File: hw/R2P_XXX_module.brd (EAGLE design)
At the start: 40 x 40 mm, 32 parts, among them U1 STM32F103CX, U5 LD3985XX, X1 MICROMATCH-4

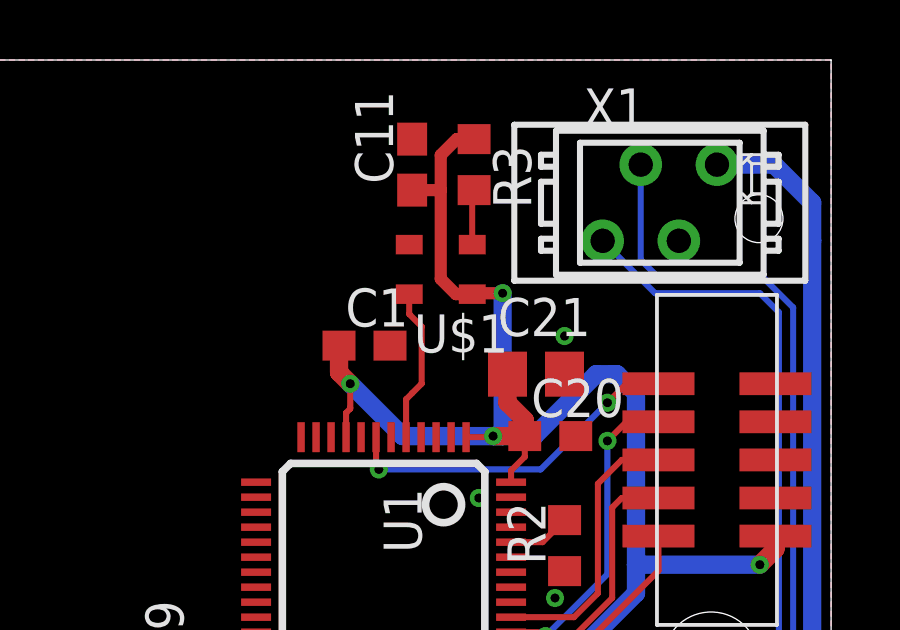
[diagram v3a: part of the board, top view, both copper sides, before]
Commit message: Clock generator moved up
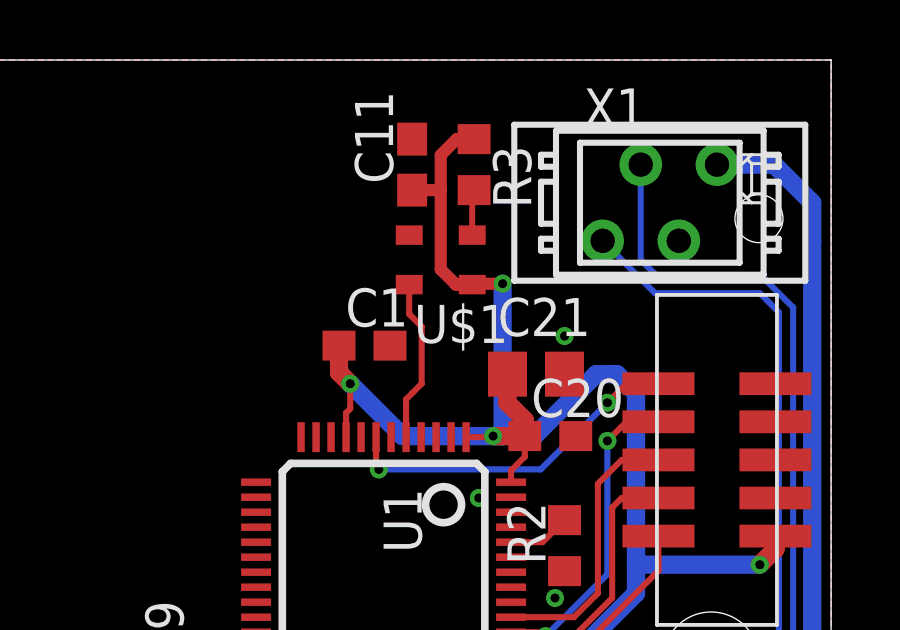
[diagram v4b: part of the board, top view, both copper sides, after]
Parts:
- moved U$1 0.32 mm to (27.0, 33.3)
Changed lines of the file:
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@@
 <element name="2" library="molex" package="0438600010" value="RJ45-43860" x="10" y="3"/>
 <element name="JP2" library="misc" package="1X04" value="" x="30.00375" y="10.4775" rot="R180"/>
-<element name="U$1" library="crystal" package="ASE" value="ASE" x="26.9875" y="33.02" rot="R180">
-<attribute name="OC_NEWARK" value="unknown" x="-26.3525" y="67.31" size="1.778" layer="27" rot="R180" display="off"/>
-<attribute name="MPN" value="" x="-26.3525" y="67.31" size="1.778" layer="27" rot="R180" display="off"/>
-<attribute name="MF" value="" x="-26.3525" y="67.31" size="1.778" layer="27" rot="R180" display="off"/>
-<attribute name="OC_FARNELL" value="unknown" x="-26.3525" y="67.31" size="1.778" layer="27" rot="R180" display="off"/>
+<element name="U$1" library="crystal" package="ASE" value="ASE" x="26.9875" y="33.3375" rot="R180">
+<attribute name="OC_NEWARK" value="unknown" x="-26.3525" y="67.6275" size="1.778" layer="27" rot="R180" display="off"/>
+<attribute name="MPN" value="" x="-26.3525" y="67.6275" size="1.778" layer="27" rot="R180" display="off"/>
+<attribute name="MF" value="" x="-26.3525" y="67.6275" size="1.778" layer="27" rot="R180" display="off"/>
+<attribute name="OC_FARNELL" value="unknown" x="-26.3525" y="67.6275" size="1.778" layer="27" rot="R180" display="off"/>
 </element>
 <element name="R2" library="rcl" package="R0603" value="10k" x="31.115" y="23.8125" rot="R90"/>
@@
 <wire x1="38.145" y1="24.01625" x2="38.145" y2="23.69875" width="0.6096" layer="1"/>
 <wire x1="38.145" y1="23.69875" x2="37.62375" y2="23.1775" width="0.6096" layer="1"/>
-<wire x1="28.0375" y1="32.195" x2="27.495" y2="32.195" width="0.4064" layer="1"/>
-<wire x1="27.495" y1="32.195" x2="26.9875" y2="32.7025" width="0.4064" layer="1"/>
-<wire x1="26.9875" y1="32.7025" x2="26.9875" y2="35.6625" width="0.4064" layer="1"/>
+<wire x1="28.0375" y1="32.5125" x2="27.495" y2="32.5125" width="0.4064" layer="1"/>
+<wire x1="27.495" y1="32.5125" x2="26.9875" y2="33.02" width="0.4064" layer="1"/>
+<wire x1="26.9875" y1="33.02" x2="26.9875" y2="35.6625" width="0.4064" layer="1"/>
 <wire x1="26.9875" y1="35.6625" x2="26.035" y2="35.6625" width="0.4064" layer="1"/>
 <wire x1="28.09875" y1="37.3625" x2="27.52" y2="37.3625" width="0.4064" layer="1"/>
@@
 <wire x1="28.73375" y1="27.46375" x2="25.7175" y2="27.46375" width="0.6096" layer="16"/>
 <wire x1="25.7175" y1="27.46375" x2="23.97125" y2="29.21" width="0.6096" layer="16"/>
-<via x="29.05125" y="32.22625" extent="1-16" drill="0.3" shape="octagon"/>
-<wire x1="28.0375" y1="32.195" x2="28.06875" y2="32.22625" width="0.4064" layer="1"/>
-<wire x1="28.06875" y1="32.22625" x2="29.05125" y2="32.22625" width="0.4064" layer="1"/>
-<wire x1="29.05125" y1="32.22625" x2="29.05125" y2="27.46375" width="0.6096" layer="16"/>
+<via x="29.05125" y="32.54375" extent="1-16" drill="0.3" shape="octagon"/>
+<wire x1="28.0375" y1="32.5125" x2="28.06875" y2="32.54375" width="0.4064" layer="1"/>
+<wire x1="28.06875" y1="32.54375" x2="29.05125" y2="32.54375" width="0.4064" layer="1"/>
+<wire x1="29.05125" y1="32.54375" x2="29.05125" y2="27.46375" width="0.6096" layer="16"/>
 <wire x1="29.05125" y1="27.46375" x2="28.73375" y2="27.46375" width="0.6096" layer="16"/>
 </signal>
@@
 <wire x1="26.3525" y1="29.21" x2="26.3525" y2="31.115" width="0.2032" layer="1"/>
 <wire x1="26.3525" y1="31.115" x2="25.9375" y2="31.53" width="0.2032" layer="1"/>
-<wire x1="25.9375" y1="31.53" x2="25.9375" y2="32.195" width="0.2032" layer="1"/>
+<wire x1="25.9375" y1="31.53" x2="25.9375" y2="32.5125" width="0.2032" layer="1"/>
 </signal>
 <signal name="OSC_OUT">
@@
 <contactref element="U$1" pad="1"/>
 <contactref element="R3" pad="2"/>
-<wire x1="28.0375" y1="33.845" x2="28.0375" y2="35.60125" width="0.2032" layer="1"/>
+<wire x1="28.0375" y1="34.1625" x2="28.0375" y2="35.60125" width="0.2032" layer="1"/>
 <wire x1="28.0375" y1="35.60125" x2="28.09875" y2="35.6625" width="0.2032" layer="1"/>
 </signal>
